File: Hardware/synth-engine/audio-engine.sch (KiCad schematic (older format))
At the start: 26 parts

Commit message: assign footprints to schematic symbols.
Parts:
- C24, C25, C26, C27, C28, C29, C30, C31, C32, C33, C34, C35, C36, C37, C38, C39: renamed from C?; footprint (none) -> SparkFun-Passives:0805
- J5: renamed from J?; footprint (none) -> SparkFun-Connectors:1X06
- R32, R33, R34, R35, R36, R37, R38: renamed from R?; footprint (none) -> SparkFun-Passives:0805
- Y2: renamed from Y?; footprint (none) -> Crystal:Crystal_SMD_HC49-SD_HandSoldering
- gave numbers to parts that had none: 1
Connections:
- net I2S_WCLK: now also U3.44 (PE13)

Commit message: add separate PCB with potentiometers and switches and connector between control board and synth engine
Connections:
- net CAD1: now also U3.39 (PE8); no longer U3.43 (PE12)
- net CSN: now also U3.43 (PE12); no longer U3.39 (PE8)
- net DIF0: now also U3.42 (PE11); no longer U3.40 (PE9)
- net DIF2: now also U3.40 (PE9); no longer U3.42 (PE11)
- net I2S_WCLK: now also U3.38 (PE7); no longer U3.44 (PE13)
- net PDN: now also U3.44 (PE13); no longer U3.38 (PE7)
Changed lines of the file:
@@
 $Descr A4 11693 8268
 encoding utf-8
-Sheet 3 6
+Sheet 3 7
 Title ""
 Date ""
@@
 Wire Wire Line
 	1700 3000 1700 3250
-Text HLabel 2800 4000 0    50   BiDi ~ 0
+Text HLabel 2800 4600 0    50   BiDi ~ 0
 PDN
 Text HLabel 4600 4300 2    50   BiDi ~ 0
@@
 Text HLabel 4600 4500 2    50   BiDi ~ 0
 I2S_LRCLK
-Text HLabel 2800 4600 0    50   BiDi ~ 0
+Text HLabel 2800 4000 0    50   BiDi ~ 0
 I2S_WCLK
-Text HLabel 2800 4100 0    50   BiDi ~ 0
+Text HLabel 2800 4500 0    50   BiDi ~ 0
 CSN
 Text HLabel 4600 3900 2    50   BiDi ~ 0
@@
 Text HLabel 4600 4000 2    50   BiDi ~ 0
 I2C_SDA
-Text HLabel 2800 4200 0    50   BiDi ~ 0
+Text HLabel 2800 4400 0    50   BiDi ~ 0
 DIF0
 Text HLabel 2800 4300 0    50   BiDi ~ 0
 DIF1
-Text HLabel 2800 4400 0    50   BiDi ~ 0
+Text HLabel 2800 4200 0    50   BiDi ~ 0
 DIF2
 Text HLabel 4600 5600 2    50   BiDi ~ 0
 MCLK
-Text HLabel 2800 4500 0    50   BiDi ~ 0
+Text HLabel 2800 4100 0    50   BiDi ~ 0
 CAD1
 Text HLabel 4600 1600 2    50   Output ~ 0

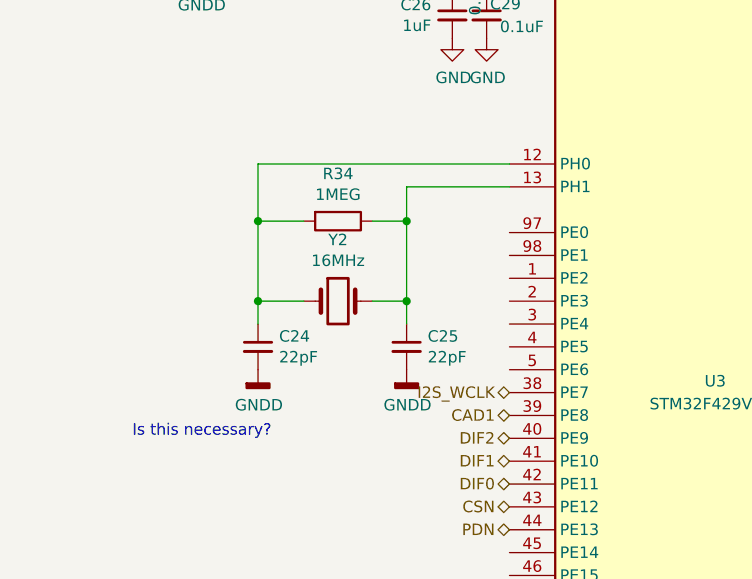
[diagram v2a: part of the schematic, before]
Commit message: initial routing complete. Still need to do ground plane pours. There are still some issues with incorrect footprints.
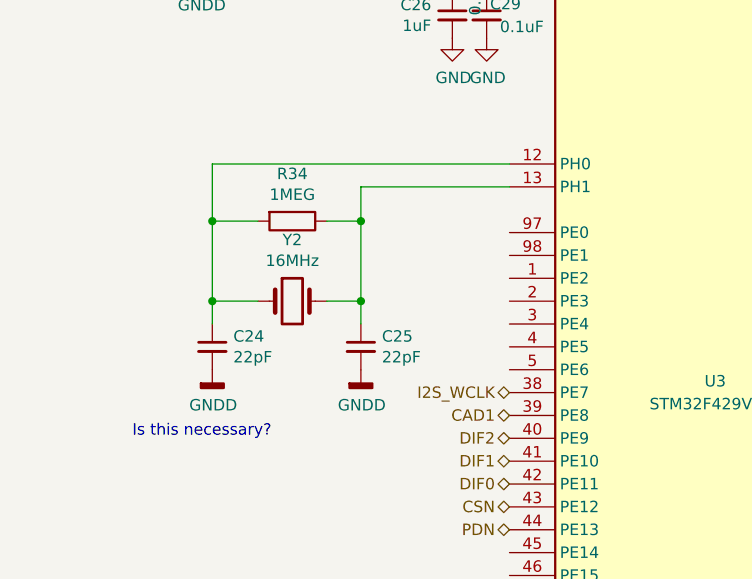
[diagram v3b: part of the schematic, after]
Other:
- moved on the sheet: C24, C25, R34, Y2
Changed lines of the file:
@@
 L Device:R R34
 U 1 1 5DDE8ED5
-P 2050 3250
-F 0 "R34" V 1843 3250 50  0000 C CNN
-F 1 "1MEG" V 1934 3250 50  0000 C CNN
-F 2 "SparkFun-Passives:0805" V 1980 3250 50  0001 C CNN
-F 3 "~" H 2050 3250 50  0001 C CNN
-	1    2050 3250
+P 1850 3250
+F 0 "R34" V 1643 3250 50  0000 C CNN
+F 1 "1MEG" V 1734 3250 50  0000 C CNN
+F 2 "SparkFun-Passives:0805" V 1780 3250 50  0001 C CNN
+F 3 "~" H 1850 3250 50  0001 C CNN
+	1    1850 3250
 	0    1    1    0
 $EndComp
@@
 L Device:C_Small C24
 U 1 1 5DDE8EDC
-P 1700 3800
-F 0 "C24" H 1792 3846 50  0000 L CNN
-F 1 "22pF" H 1792 3755 50  0000 L CNN
-F 2 "SparkFun-Passives:0805" H 1700 3800 50  0001 C CNN
-F 3 "~" H 1700 3800 50  0001 C CNN
-	1    1700 3800
+P 1500 3800
+F 0 "C24" H 1592 3846 50  0000 L CNN
+F 1 "22pF" H 1592 3755 50  0000 L CNN
+F 2 "SparkFun-Passives:0805" H 1500 3800 50  0001 C CNN
+F 3 "~" H 1500 3800 50  0001 C CNN
+	1    1500 3800
 	1    0    0    -1
 $EndComp
@@
 L Device:C_Small C25
 U 1 1 5DDE8EE3
-P 2350 3800
-F 0 "C25" H 2442 3846 50  0000 L CNN
-F 1 "22pF" H 2442 3755 50  0000 L CNN
-F 2 "SparkFun-Passives:0805" H 2350 3800 50  0001 C CNN
-F 3 "~" H 2350 3800 50  0001 C CNN
-	1    2350 3800
+P 2150 3800
+F 0 "C25" H 2242 3846 50  0000 L CNN
+F 1 "22pF" H 2242 3755 50  0000 L CNN
+F 2 "SparkFun-Passives:0805" H 2150 3800 50  0001 C CNN
+F 3 "~" H 2150 3800 50  0001 C CNN
+	1    2150 3800
 	1    0    0    -1
 $EndComp
@@
 L Device:Crystal Y?
 U 1 1 5DDE8EEA
-P 2050 3600
+P 1850 3600
 AR Path="/5DDBDEEA/5DDE8EEA" Ref="Y?"  Part="1"
 AR Path="/5DDC7BB6/5DDE8EEA" Ref="Y2"  Part="1"
-F 0 "Y2" H 2050 3868 50  0000 C CNN
-F 1 "16MHz" H 2050 3777 50  0000 C CNN
-F 2 "Crystal:Crystal_SMD_HC49-SD_HandSoldering" H 2050 3600 50  0001 C CNN
-F 3 "~" H 2050 3600 50  0001 C CNN
-	1    2050 3600
+F 0 "Y2" H 1850 3868 50  0000 C CNN
+F 1 "16MHz" H 1850 3777 50  0000 C CNN
+F 2 "Crystal:Crystal_SMD_HC49-SD_HandSoldering" H 1850 3600 50  0001 C CNN
+F 3 "~" H 1850 3600 50  0001 C CNN
+	1    1850 3600
 	1    0    0    -1
 $EndComp
 Wire Wire Line
-	2350 3700 2350 3600
+	2150 3700 2150 3600
 Wire Wire Line
-	2350 3250 2200 3250
+	2150 3250 2000 3250
 Wire Wire Line
-	2200 3600 2350 3600
-Connection ~ 2350 3600
+	2000 3600 2150 3600
+Connection ~ 2150 3600
 Wire Wire Line
-	2350 3600 2350 3250
+	2150 3600 2150 3250
 Wire Wire Line
-	1900 3250 1700 3250
+	1700 3250 1500 3250
 Wire Wire Line
-	1700 3250 1700 3600
+	1500 3250 1500 3600
 $Comp
 L power:GNDD #PWR045
 U 1 1 5DDE8EF8
-P 1700 3900
-F 0 "#PWR045" H 1700 3650 50  0001 C CNN
-F 1 "GNDD" H 1704 3745 50  0000 C CNN
-F 2 "" H 1700 3900 50  0001 C CNN
-F 3 "" H 1700 3900 50  0001 C CNN
-	1    1700 3900
+P 1500 3900
+F 0 "#PWR045" H 1500 3650 50  0001 C CNN
+F 1 "GNDD" H 1504 3745 50  0000 C CNN
+F 2 "" H 1500 3900 50  0001 C CNN
+F 3 "" H 1500 3900 50  0001 C CNN
+	1    1500 3900
 	1    0    0    -1
 $EndComp
@@
 L power:GNDD #PWR047
 U 1 1 5DDE8EFE
-P 2350 3900
-F 0 "#PWR047" H 2350 3650 50  0001 C CNN
-F 1 "GNDD" H 2354 3745 50  0000 C CNN
-F 2 "" H 2350 3900 50  0001 C CNN
-F 3 "" H 2350 3900 50  0001 C CNN
-	1    2350 3900
+P 2150 3900
+F 0 "#PWR047" H 2150 3650 50  0001 C CNN
+F 1 "GNDD" H 2154 3745 50  0000 C CNN
+F 2 "" H 2150 3900 50  0001 C CNN
+F 3 "" H 2150 3900 50  0001 C CNN
+	1    2150 3900
 	1    0    0    -1
 $EndComp
 Wire Wire Line
-	1900 3600 1700 3600
-Connection ~ 1700 3600
+	1700 3600 1500 3600
+Connection ~ 1500 3600
 Wire Wire Line
-	1700 3600 1700 3700
+	1500 3600 1500 3700
 Wire Wire Line
-	2350 3100 2350 3250
-Connection ~ 2350 3250
-Connection ~ 1700 3250
+	2150 3100 2150 3250
+Connection ~ 2150 3250
+Connection ~ 1500 3250
 Text Notes 1150 4200 0    50   ~ 0
 Is this necessary?
 Wire Wire Line
-	2800 3100 2350 3100
+	2800 3100 2150 3100
 Wire Wire Line
-	2800 3000 1700 3000
+	2800 3000 1500 3000
 Wire Wire Line
-	1700 3000 1700 3250
+	1500 3000 1500 3250
 Text HLabel 2800 4600 0    50   BiDi ~ 0
 PDN
